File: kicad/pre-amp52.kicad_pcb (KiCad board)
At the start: 2 copper layers, 124.5 x 78.7 mm, 116 parts, among them J1 Left, J10 L out, J11 R out, J12 +12V in, J13 0V in, J14 I2C In, J15 +5V in, J16 Rpi GPIO in, J2 LFront, J3 LRear, J4 Centre, J5 RRear, J6 RFront, J7 Right, J8 Ltape, J9 Rtape, K1 G6SK-2 DC12, Q1 BC546, Q2 BC546, Q3 BC546, Q4 BC556, U1 OPA2134, U2 DS1882E, U3 DS1882E, U4 DS1882E, U5 OPA2134, U6 DS1882E, U7 OPA2134, U8 B1212S

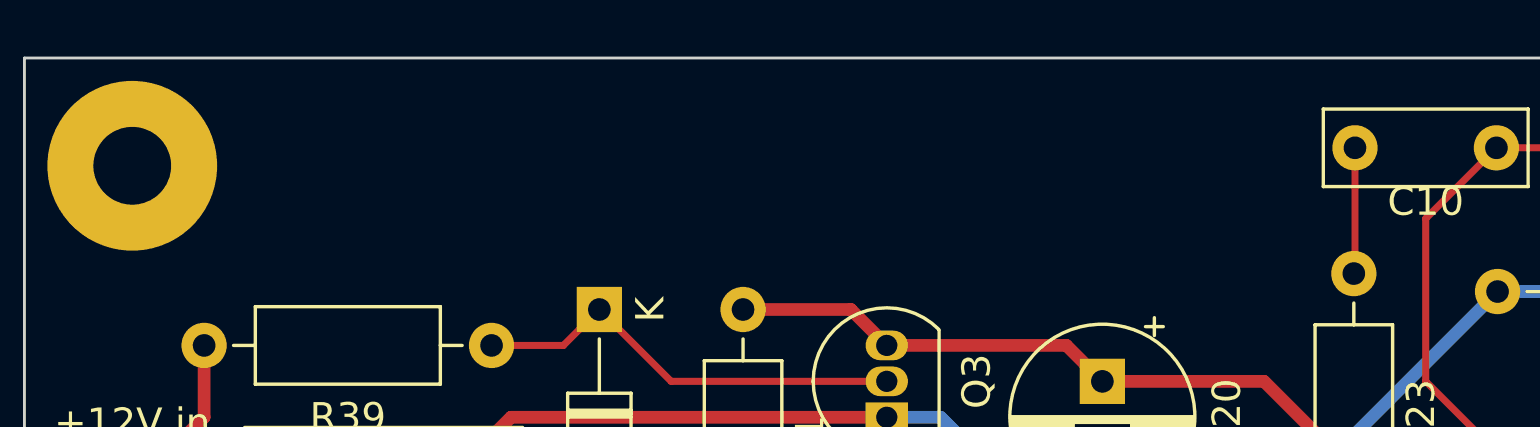
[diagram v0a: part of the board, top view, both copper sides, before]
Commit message: Added github URLs to PCB
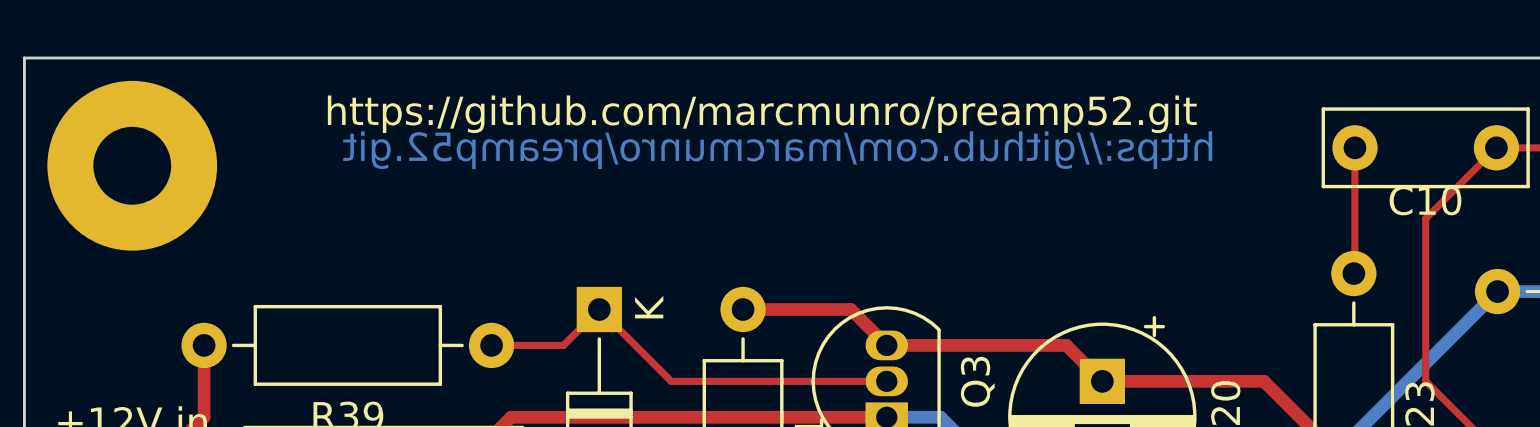
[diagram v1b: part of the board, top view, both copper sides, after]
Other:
- board text added: "https://github.com/marcmunro/preamp52.git"
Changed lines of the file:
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@@
   (gr_rect (start 45.72 83.82) (end 170.18 162.56) (layer "Edge.Cuts") (width 0.1) (fill none))
   (gr_rect (start 165.1 162.56) (end 165.1 162.56) (layer "Edge.Cuts") (width 0.1) (fill none))
+  (gr_text "https://github.com/marcmunro/preamp52.git" (at 72.39 86.995) (layer "B.Cu")
+    (effects (font (size 1 1) (thickness 0.2)) (justify mirror))
+  )
+  (gr_text "https://github.com/marcmunro/preamp52.git" (at 71.755 85.725) (layer "F.SilkS")
+    (effects (font (size 1 1) (thickness 0.15)))
+  )
   (gr_text "Preamp 52" (at 71.755 116.205) (layer "F.SilkS")
     (effects (font (size 2 2) (thickness 0.15)))

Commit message: Created schematic pdf and gerber files for pcb.
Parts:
- R1, R10, R11, R12, R13, R14, R15, R16, R17, R18, R19, R2, R20, R21, R22, R23, R24, R25, R26, R27, R28, R29, R3, R30, R31, R32, R33, R34, R35, R36, R37, R38, R39, R4, R40, R41, R42, R43, R44, R45, R46, R5, R6, R7, R8, R9: footprint Resistor_THT:R_Axial_DIN0207_L6.3mm_D2.5mm_P10.16mm_Horizontal -> my_extras:R_Axial_DIN0207_L6.3mm_D2.5mm_P10.16mm_Horizontal
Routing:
- net /PSU and control/SCL: track 132.5 -> 129.8 mm
- added copper zone on F.Cu, net GND
